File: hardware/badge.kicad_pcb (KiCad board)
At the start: 2 copper layers, 151.5 x 81.5 mm, 52 parts, among them J1 Micro_SD_Card, J2 Conn_01x40, J3 Conn_01x40, SW1 SW_Push, SW10 SW_Push, SW11 SW_Push, SW12 SW_Push, SW13 SW_Push, SW14 SW_Push, SW15 SW_Push, SW16 SW_Push, SW17 SW_Push, SW18 SW_Push, SW19 SW_Push, SW2 SW_Push, SW20 SW_Push, SW21 SW_Push, SW22 SW_Push, SW23 SW_Push, SW24 SW_Push, SW25 SW_Push, SW26 SW_Push, SW27 SW_Push, SW28 SW_Push, SW29 SW_Push, SW3 SW_Push, SW30 SW_Push, SW31 SW_Push, SW32 SW_Push, SW33 SW_Push, SW34 SW_Push, SW35 SW_Push, SW36 SW_Push, SW37 SW_Push, SW38 SW_Push, SW39 SW_Push, SW4 SW_Push, SW40 SW_Push, SW5 SW_Push, SW6 SW_Push, SW7 SW_Push, SW8 SW_Push, SW9 SW_Push, U1 ESP32-S3-WROOM-1

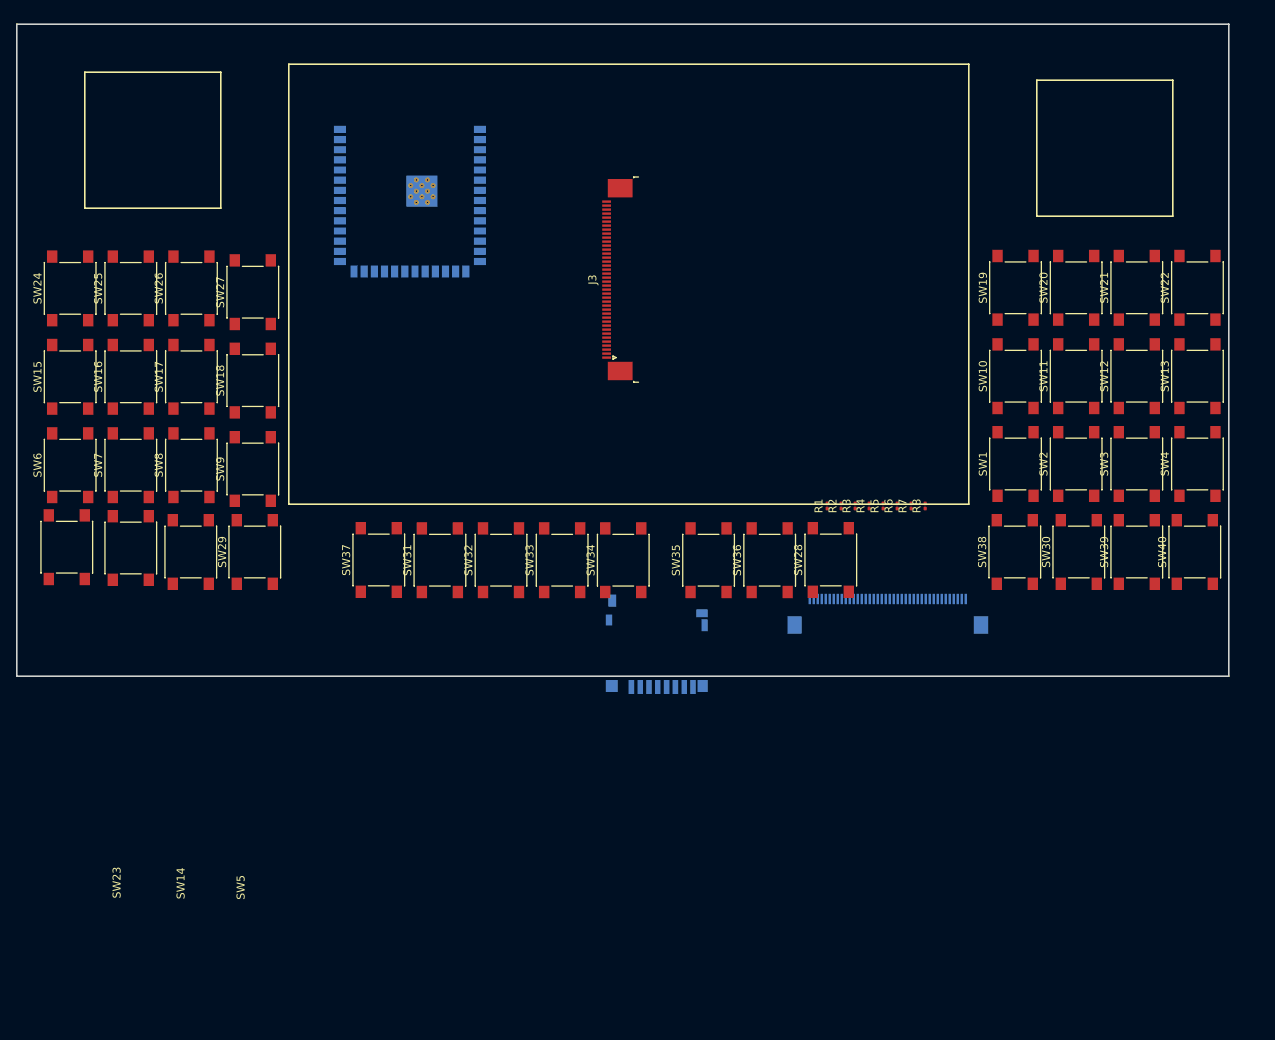
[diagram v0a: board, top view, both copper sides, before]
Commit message: display, switches, (switch)joystick footprint
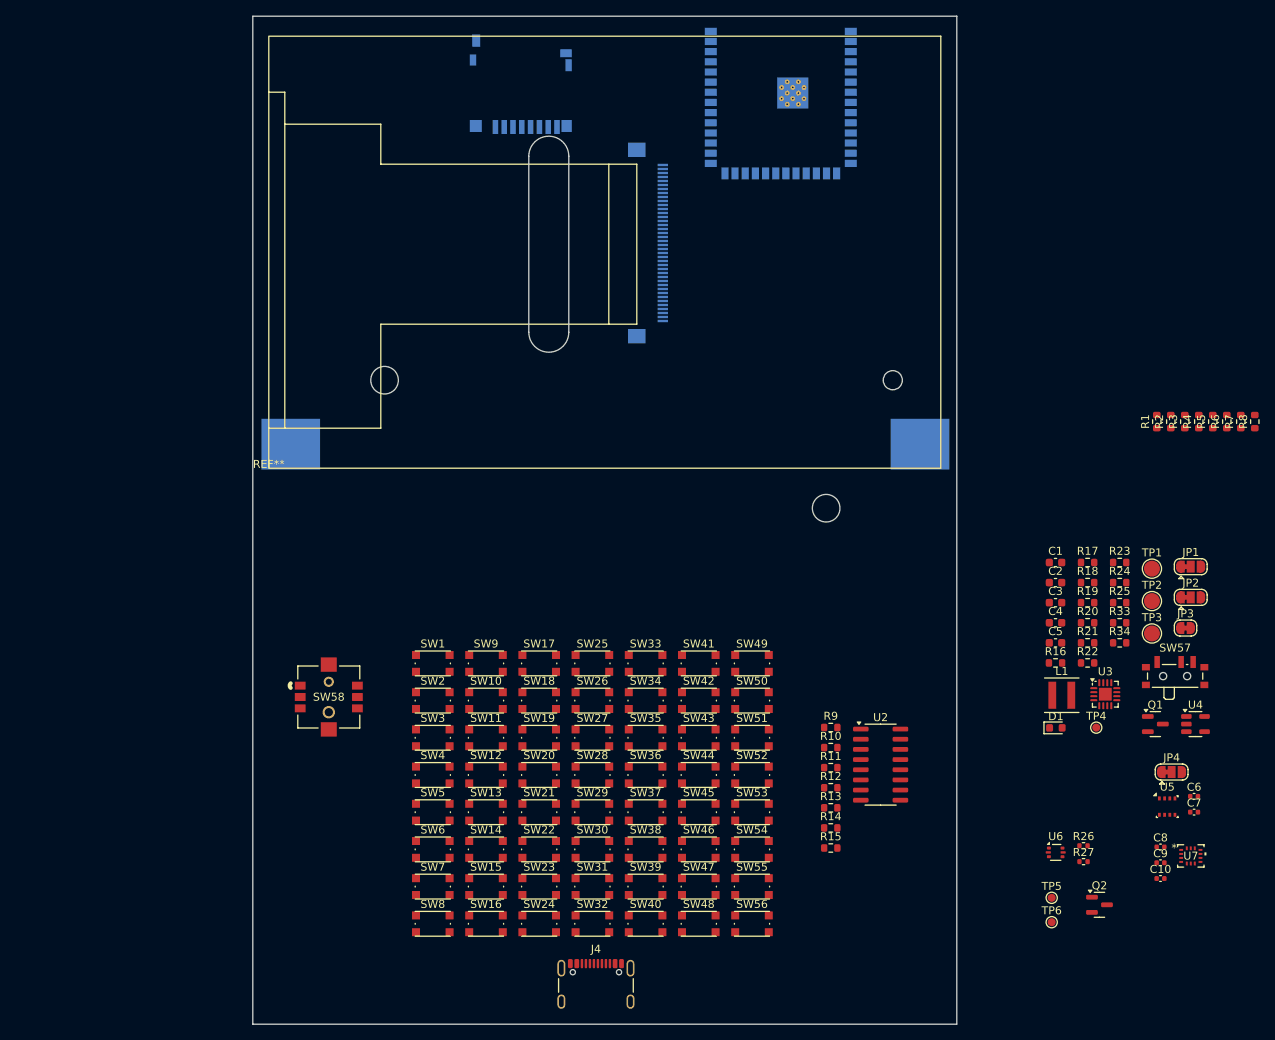
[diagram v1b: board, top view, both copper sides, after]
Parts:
- added C1: 4.7uF, Capacitor_SMD:C_0603_1608Metric, F.Cu at (181.3, 99.3)
- added C10: 100nF 6.3V, Capacitor_SMD:C_0402_1005Metric, F.Cu at (194.5, 138.8)
- added C2: TBD, Capacitor_SMD:C_0603_1608Metric, F.Cu at (181.3, 101.8)
- added C3: 4.7uF, Capacitor_SMD:C_0603_1608Metric, F.Cu at (181.3, 104.3)
- added C4: 10uF, Capacitor_SMD:C_0603_1608Metric, F.Cu at (181.3, 106.8)
- added C5: 4.7uF, Capacitor_SMD:C_0603_1608Metric, F.Cu at (181.3, 109.3)
- added C6: 100nF 6.3V, Capacitor_SMD:C_0402_1005Metric, F.Cu at (198.7, 128.5)
- added C7: 100nF 6.3V, Capacitor_SMD:C_0402_1005Metric, F.Cu at (198.7, 130.5)
- added C8: 1uF 25V, Capacitor_SMD:C_0402_1005Metric, F.Cu at (194.5, 134.8)
- added C9: 100nF 6.3V, Capacitor_SMD:C_0402_1005Metric, F.Cu at (194.5, 136.8)
- added D1: LED, LED_SMD:LED_0603_1608Metric, F.Cu at (181.4, 120.0)
- added J4: USB_C_Receptacle_USB2.0_14P, Connector_USB:USB_C_Receptacle_GCT_USB4105-xx-A_16P_TopMnt_Horizontal, F.Cu at (123.9, 153.1)
- added JP1: EN1, Jumper:SolderJumper-3_P1.3mm_Bridged12_RoundedPad1.0x1.5mm, F.Cu at (198.2, 99.8)
- added JP2: EN2, Jumper:SolderJumper-3_P1.3mm_Bridged12_RoundedPad1.0x1.5mm, F.Cu at (198.2, 103.6)
- added JP3: Grumpy wifasoi jumper, Jumper:SolderJumper-2_P1.3mm_Bridged_RoundedPad1.0x1.5mm, F.Cu at (197.6, 107.5)
- added JP4: SolderJumper_3_Bridged12, Jumper:SolderJumper-3_P1.3mm_Bridged12_RoundedPad1.0x1.5mm, F.Cu at (195.9, 125.5)
- added L1: 2.2uH, Inductor_SMD:L_Coilcraft_XxL4040, F.Cu at (182.1, 115.9)
- added Q1: NPN SS8050, Package_TO_SOT_SMD:SOT-23, F.Cu at (193.8, 119.5)
- added Q2: AO3400A, Package_TO_SOT_SMD:SOT-23, F.Cu at (186.8, 142.1)
- added R10: 22, Resistor_SMD:R_0603_1608Metric, F.Cu at (153.2, 122.4)
- added R11: 22, Resistor_SMD:R_0603_1608Metric, F.Cu at (153.2, 124.9)
- added R12: 22, Resistor_SMD:R_0603_1608Metric, F.Cu at (153.2, 127.4)
- added R13: 22, Resistor_SMD:R_0603_1608Metric, F.Cu at (153.2, 130.0)
- added R14: 22, Resistor_SMD:R_0603_1608Metric, F.Cu at (153.2, 132.5)
- added R15: 22, Resistor_SMD:R_0603_1608Metric, F.Cu at (153.2, 135.0)
- added R16: 0R, Resistor_SMD:R_0603_1608Metric, F.Cu at (181.3, 111.8)
- added R17: TBD, Resistor_SMD:R_0603_1608Metric, F.Cu at (185.4, 99.3)
- added R18: TBD, Resistor_SMD:R_0603_1608Metric, F.Cu at (185.4, 101.8)
- added R19: 10k, Resistor_SMD:R_0603_1608Metric, F.Cu at (185.4, 104.3)
- added R20: 10k, Resistor_SMD:R_0603_1608Metric, F.Cu at (185.4, 106.8)
- added R21: 680k, Resistor_SMD:R_0603_1608Metric, F.Cu at (185.4, 109.3)
- added R22: 150K, Resistor_SMD:R_0603_1608Metric, F.Cu at (185.4, 111.8)
- added R23: 330, Resistor_SMD:R_0603_1608Metric, F.Cu at (189.4, 99.3)
- added R24: 10k, Resistor_SMD:R_0603_1608Metric, F.Cu at (189.4, 101.8)
- added R25: 10k, Resistor_SMD:R_0603_1608Metric, F.Cu at (189.4, 104.3)
- added R26: 5k1, Resistor_SMD:R_0402_1005Metric, F.Cu at (184.8, 134.7)
- added R27: 5k1, Resistor_SMD:R_0402_1005Metric, F.Cu at (184.8, 136.7)
- added R33: 150K, Resistor_SMD:R_0603_1608Metric, F.Cu at (189.4, 106.8)
- added R34: 150K, Resistor_SMD:R_0603_1608Metric, F.Cu at (189.4, 109.3)
- added R9: 22, Resistor_SMD:R_0603_1608Metric, F.Cu at (153.2, 119.9)
- added REF**: display, lib:display, F.Cu at (83.0, 87.5)
- added SW41: SW_Push, lib:bottonepiccolo_C2888430, F.Cu at (136.8, 111.9)
- added SW42: SW_Push, lib:bottonepiccolo_C2888430, F.Cu at (136.8, 116.5)
- added SW43: SW_Push, lib:bottonepiccolo_C2888430, F.Cu at (136.8, 121.2)
- added SW44: SW_Push, lib:bottonepiccolo_C2888430, F.Cu at (136.8, 125.8)
- added SW45: SW_Push, lib:bottonepiccolo_C2888430, F.Cu at (136.8, 130.5)
- added SW46: SW_Push, lib:bottonepiccolo_C2888430, F.Cu at (136.8, 135.2)
- added SW47: SW_Push, lib:bottonepiccolo_C2888430, F.Cu at (136.8, 139.8)
- added SW48: SW_Push, lib:bottonepiccolo_C2888430, F.Cu at (136.8, 144.4)
- added SW49: SW_Push, lib:bottonepiccolo_C2888430, F.Cu at (143.4, 111.9)
- added SW50: SW_Push, lib:bottonepiccolo_C2888430, F.Cu at (143.4, 116.5)
- added SW51: SW_Push, lib:bottonepiccolo_C2888430, F.Cu at (143.4, 121.2)
- added SW52: SW_Push, lib:bottonepiccolo_C2888430, F.Cu at (143.4, 125.8)
- added SW53: SW_Push, lib:bottonepiccolo_C2888430, F.Cu at (143.4, 130.5)
- added SW54: SW_Push, lib:bottonepiccolo_C2888430, F.Cu at (143.4, 135.2)
- added SW55: SW_Push, lib:bottonepiccolo_C2888430, F.Cu at (143.4, 139.8)
- added SW56: SW_Push, lib:bottonepiccolo_C2888430, F.Cu at (143.4, 144.4)
- added SW57: MK-12C02-G020, Button_Switch_SMD:SW_SPDT_PCM12, F.Cu at (196.3, 113.2)
- added SW58: SKRHABE010, lib:SKRHABE010_ALPS, F.Cu at (90.5, 116.1)
- added TP1: TestPoint, TestPoint:TestPoint_Pad_D2.0mm, F.Cu at (193.4, 100.1)
- added TP2: TestPoint, TestPoint:TestPoint_Pad_D2.0mm, F.Cu at (193.4, 104.1)
- added TP3: TestPoint, TestPoint:TestPoint_Pad_D2.0mm, F.Cu at (193.4, 108.2)
- added TP4: TestPoint, TestPoint:TestPoint_Pad_D1.0mm, F.Cu at (186.4, 119.9)
- added TP5: TestPoint, TestPoint:TestPoint_Pad_D1.0mm, F.Cu at (180.9, 141.2)
- added TP6: TestPoint, TestPoint:TestPoint_Pad_D1.0mm, F.Cu at (180.9, 144.2)
- added U2: 74HC138, Package_SO:SOIC-16_3.9x9.9mm_P1.27mm, F.Cu at (159.5, 124.6)
- added U3: BQ24075RGT, Package_DFN_QFN:VQFN-16-1EP_3x3mm_P0.5mm_EP1.6x1.6mm, F.Cu at (187.6, 115.8)
- added U4: TLV62569DBV, Package_TO_SOT_SMD:SOT-23-5, F.Cu at (198.8, 119.5)
- added U5: BME280, Package_LGA:Bosch_LGA-8_2.5x2.5mm_P0.65mm_ClockwisePinNumbering, F.Cu at (195.3, 129.8)
- added U6: USBLC6-2P6, Package_TO_SOT_SMD:SOT-666, F.Cu at (181.4, 135.5)
- added U7: BMI270, footprints:BMI270_BOS, F.Cu at (198.3, 136.0)
- J2: value Conn_01x40 -> batt; footprint Connector_FFC-FPC:Hirose_FH12-40S-0.5SH_1x40-1MP_P0.50mm_Horizontal -> Battery:BatteryHolder_Keystone_1042_1x18650
- J3: footprint Connector_FFC-FPC:TE_4-1734839-0_1x40-1MP_P0.5mm_Horizontal -> Connector_FFC-FPC:Hirose_FH12-40S-0.5SH_1x40-1MP_P0.50mm_Horizontal; moved to B.Cu
- R1, R2: value R -> 10k; footprint Resistor_SMD:R_0201_0603Metric -> Resistor_SMD:R_0603_1608Metric
- R3, R4, R5, R6, R7: footprint Resistor_SMD:R_0201_0603Metric -> Resistor_SMD:R_0603_1608Metric
- R8: value 10k -> 22; footprint Resistor_SMD:R_0201_0603Metric -> Resistor_SMD:R_0603_1608Metric
- SW1, SW10, SW11, SW12, SW13, SW14, SW15, SW16, SW17, SW18, SW19, SW2, SW20, SW21, SW22, SW23, SW24, SW25, SW26, SW27, SW28, SW29, SW3, SW30, SW31, SW32, SW33, SW34, SW35, SW36, SW37, SW38, SW39, SW4, SW40, SW5, SW6, SW7, SW8, SW9: footprint Button_Switch_SMD:SW_Push_1P1T_NO_6x6mm_H9.5mm -> lib:bottonepiccolo_C2888430
- moved SW22 108.2 mm to (116.8, 135.2), turned to 0 degrees
- moved SW13 104.3 mm to (110.2, 130.5), turned to 0 degrees
- moved SW4 103.2 mm to (103.5, 125.8), turned to 0 degrees
- moved SW21 99.4 mm to (116.8, 130.5), turned to 0 degrees
- moved SW24 98.7 mm to (116.8, 144.4), turned to 0 degrees
- moved SW12 95.4 mm to (110.2, 125.8), turned to 0 degrees
- moved SW3 94.4 mm to (103.5, 121.2), turned to 0 degrees
- moved SW20 90.6 mm to (116.8, 125.8), turned to 0 degrees
- moved SW11 86.5 mm to (110.2, 121.2), turned to 0 degrees
- moved SW2 85.7 mm to (103.5, 116.5), turned to 0 degrees
- moved SW40 82.9 mm to (130.1, 144.4), turned to 0 degrees
- moved SW15 82.2 mm to (110.2, 139.8), turned to 0 degrees
- moved SW19 81.9 mm to (116.8, 121.2), turned to 0 degrees
- moved SW16 81.5 mm to (110.2, 144.4), turned to 0 degrees
- moved SW10 77.6 mm to (110.2, 116.5), turned to 0 degrees
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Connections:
- J2 pad 1: unconnected-(J2-Pin_1-Pad1) -> GND
- J2 pad 2: unconnected-(J2-Pin_2-Pad2) -> Net-(J2-Pin_2)
- J3 pad 10: unconnected-(J3-Pin_10-Pad10) -> GND
- J3 pad 11: unconnected-(J3-Pin_11-Pad11) -> /lcd/SPI_CLK
- J3 pad 12: unconnected-(J3-Pin_12-Pad12) -> GND
- J3 pad 13: unconnected-(J3-Pin_13-Pad13) -> /lcd/SPI_MOSI
- J3 pad 14: unconnected-(J3-Pin_14-Pad14) -> /lcd/SPI_MISO
- J3 pad 15: unconnected-(J3-Pin_15-Pad15) -> GND
- J3 pad 16: unconnected-(J3-Pin_16-Pad16) -> GND
- J3 pad 17: unconnected-(J3-Pin_17-Pad17) -> GND
- J3 pad 18: unconnected-(J3-Pin_18-Pad18) -> GND
- J3 pad 19: unconnected-(J3-Pin_19-Pad19) -> GND
- J3 pad 20: unconnected-(J3-Pin_20-Pad20) -> GND
- J3 pad 21: unconnected-(J3-Pin_21-Pad21) -> GND
- J3 pad 22: unconnected-(J3-Pin_22-Pad22) -> GND
- J3 pad 23: unconnected-(J3-Pin_23-Pad23) -> GND
- J3 pad 24: unconnected-(J3-Pin_24-Pad24) -> GND
- J3 pad 25: unconnected-(J3-Pin_25-Pad25) -> GND
- J3 pad 26: unconnected-(J3-Pin_26-Pad26) -> GND
- J3 pad 27: unconnected-(J3-Pin_27-Pad27) -> GND
- J3 pad 28: unconnected-(J3-Pin_28-Pad28) -> GND
- J3 pad 29: unconnected-(J3-Pin_29-Pad29) -> GND
- J3 pad 30: unconnected-(J3-Pin_30-Pad30) -> GND
- J3 pad 31: unconnected-(J3-Pin_31-Pad31) -> GND
- J3 pad 32: unconnected-(J3-Pin_32-Pad32) -> GND
- J3 pad 33: unconnected-(J3-Pin_33-Pad33) -> +3.3V
- J3 pad 34: unconnected-(J3-Pin_34-Pad34) -> /lcd/LEDK
- J3 pad 35: unconnected-(J3-Pin_35-Pad35) -> /lcd/LEDK
- J3 pad 36: unconnected-(J3-Pin_36-Pad36) -> /lcd/LEDK
- J3 pad 37: unconnected-(J3-Pin_37-Pad37) -> GND
- J3 pad 38: unconnected-(J3-Pin_38-Pad38) -> /lcd/IM0
- J3 pad 39: unconnected-(J3-Pin_39-Pad39) -> /lcd/IM1
- J3 pad 40: unconnected-(J3-Pin_40-Pad40) -> /lcd/IM2
- J3 pad 5: unconnected-(J3-Pin_5-Pad5) -> GND
- J3 pad 6: unconnected-(J3-Pin_6-Pad6) -> +3.3V
- J3 pad 7: unconnected-(J3-Pin_7-Pad7) -> +3.3V
- J3 pad 8: unconnected-(J3-Pin_8-Pad8) -> /lcd/FMARK
- J3 pad 9: unconnected-(J3-Pin_9-Pad9) -> /lcd/SPI_CS
- R1 pad 1: Net-(J3-CC1) -> +3.3V
- R1 pad 2: GND -> Net-(U1-EN)
- R2 pad 1: Net-(J3-CC2) -> +3.3V
- R2 pad 2: GND -> Net-(J1-DAT1)
- R3 pad 2: Net-(J1-DAT1) -> /mcu/SD_D0
- R4 pad 2: /mcu/SD_D0 -> /mcu/SD_CLK
- R5 pad 2: /mcu/SD_CLK -> /mcu/SD_CMD
- R6 pad 2: /mcu/SD_CMD -> Net-(J1-DAT3/CD)
- R7 pad 2: Net-(J1-DAT3/CD) -> Net-(J1-DAT2)
- R8 pad 1: +3.3V -> Net-(U2-~{Y0})
- R8 pad 2: Net-(J1-DAT2) -> Net-(R8-Pad2)
- SW1 pad 1: unconnected-(SW1-Pad1) -> Net-(R8-Pad2)
- SW1 pad 2: unconnected-(SW1-Pad2) -> /keyboard/KB_COL0
- SW10 pad 1: unconnected-(SW10-Pad1) -> Net-(R9-Pad2)
- SW10 pad 2: unconnected-(SW10-Pad2) -> /keyboard/KB_COL1
- SW11 pad 1: unconnected-(SW11-Pad1) -> Net-(R10-Pad2)
- SW11 pad 2: unconnected-(SW11-Pad2) -> /keyboard/KB_COL1
- SW12 pad 1: unconnected-(SW12-Pad1) -> Net-(R11-Pad2)
- SW12 pad 2: unconnected-(SW12-Pad2) -> /keyboard/KB_COL1
- SW13 pad 1: unconnected-(SW13-Pad1) -> Net-(R12-Pad2)
- SW13 pad 2: unconnected-(SW13-Pad2) -> /keyboard/KB_COL1
- SW14 pad 1: unconnected-(SW14-Pad1) -> Net-(R13-Pad2)
- SW14 pad 2: unconnected-(SW14-Pad2) -> /keyboard/KB_COL1
- SW15 pad 1: unconnected-(SW15-Pad1) -> Net-(R14-Pad2)
- SW15 pad 2: unconnected-(SW15-Pad2) -> /keyboard/KB_COL1
- SW16 pad 1: unconnected-(SW16-Pad1) -> Net-(R15-Pad2)
- SW16 pad 2: unconnected-(SW16-Pad2) -> /keyboard/KB_COL1
- SW17 pad 1: unconnected-(SW17-Pad1) -> Net-(R8-Pad2)
- SW17 pad 2: unconnected-(SW17-Pad2) -> /keyboard/KB_COL2
- SW18 pad 1: unconnected-(SW18-Pad1) -> Net-(R9-Pad2)
- SW18 pad 2: unconnected-(SW18-Pad2) -> /keyboard/KB_COL2
- SW19 pad 1: unconnected-(SW19-Pad1) -> Net-(R10-Pad2)
- SW19 pad 2: unconnected-(SW19-Pad2) -> /keyboard/KB_COL2
- SW2 pad 1: unconnected-(SW2-Pad1) -> Net-(R9-Pad2)
- SW2 pad 2: unconnected-(SW2-Pad2) -> /keyboard/KB_COL0
- SW20 pad 1: unconnected-(SW20-Pad1) -> Net-(R11-Pad2)
- SW20 pad 2: unconnected-(SW20-Pad2) -> /keyboard/KB_COL2
- SW21 pad 1: unconnected-(SW21-Pad1) -> Net-(R12-Pad2)
- SW21 pad 2: unconnected-(SW21-Pad2) -> /keyboard/KB_COL2
- SW22 pad 1: unconnected-(SW22-Pad1) -> Net-(R13-Pad2)
- SW22 pad 2: unconnected-(SW22-Pad2) -> /keyboard/KB_COL2
- SW23 pad 1: unconnected-(SW23-Pad1) -> Net-(R14-Pad2)
- SW23 pad 2: unconnected-(SW23-Pad2) -> /keyboard/KB_COL2
- SW24 pad 1: unconnected-(SW24-Pad1) -> Net-(R15-Pad2)
- SW24 pad 2: unconnected-(SW24-Pad2) -> /keyboard/KB_COL2
- SW25 pad 1: unconnected-(SW25-Pad1) -> Net-(R8-Pad2)
- SW25 pad 2: unconnected-(SW25-Pad2) -> /keyboard/KB_COL3
- SW26 pad 1: unconnected-(SW26-Pad1) -> Net-(R9-Pad2)
- SW26 pad 2: unconnected-(SW26-Pad2) -> /keyboard/KB_COL3
- SW27 pad 1: unconnected-(SW27-Pad1) -> Net-(R10-Pad2)
- SW27 pad 2: unconnected-(SW27-Pad2) -> /keyboard/KB_COL3
- SW28 pad 1: unconnected-(SW28-Pad1) -> Net-(R11-Pad2)
- SW28 pad 2: unconnected-(SW28-Pad2) -> /keyboard/KB_COL3
- SW29 pad 1: unconnected-(SW29-Pad1) -> Net-(R12-Pad2)
- SW29 pad 2: unconnected-(SW29-Pad2) -> /keyboard/KB_COL3
- SW3 pad 1: unconnected-(SW3-Pad1) -> Net-(R10-Pad2)
- SW3 pad 2: unconnected-(SW3-Pad2) -> /keyboard/KB_COL0
- SW30 pad 1: unconnected-(SW30-Pad1) -> Net-(R13-Pad2)
- SW30 pad 2: unconnected-(SW30-Pad2) -> /keyboard/KB_COL3
- SW31 pad 1: unconnected-(SW31-Pad1) -> Net-(R14-Pad2)
- SW31 pad 2: unconnected-(SW31-Pad2) -> /keyboard/KB_COL3
- SW32 pad 1: unconnected-(SW32-Pad1) -> Net-(R15-Pad2)
- SW32 pad 2: unconnected-(SW32-Pad2) -> /keyboard/KB_COL3
- SW33 pad 1: unconnected-(SW33-Pad1) -> Net-(R8-Pad2)
- SW33 pad 2: unconnected-(SW33-Pad2) -> /keyboard/KB_COL4
- SW34 pad 1: unconnected-(SW34-Pad1) -> Net-(R9-Pad2)
- SW34 pad 2: unconnected-(SW34-Pad2) -> /keyboard/KB_COL4
- SW35 pad 1: unconnected-(SW35-Pad1) -> Net-(R10-Pad2)
- SW35 pad 2: unconnected-(SW35-Pad2) -> /keyboard/KB_COL4
- SW36 pad 1: unconnected-(SW36-Pad1) -> Net-(R11-Pad2)
- SW36 pad 2: unconnected-(SW36-Pad2) -> /keyboard/KB_COL4
- SW37 pad 1: unconnected-(SW37-Pad1) -> Net-(R12-Pad2)
- SW37 pad 2: unconnected-(SW37-Pad2) -> /keyboard/KB_COL4
- SW38 pad 1: unconnected-(SW38-Pad1) -> Net-(R13-Pad2)
- SW38 pad 2: unconnected-(SW38-Pad2) -> /keyboard/KB_COL4
- SW39 pad 1: unconnected-(SW39-Pad1) -> Net-(R14-Pad2)
- SW39 pad 2: unconnected-(SW39-Pad2) -> /keyboard/KB_COL4
- SW4 pad 1: unconnected-(SW4-Pad1) -> Net-(R11-Pad2)
- SW4 pad 2: unconnected-(SW4-Pad2) -> /keyboard/KB_COL0
- SW40 pad 1: unconnected-(SW40-Pad1) -> Net-(R15-Pad2)
- SW40 pad 2: unconnected-(SW40-Pad2) -> /keyboard/KB_COL4
- SW5 pad 1: unconnected-(SW5-Pad1) -> Net-(R12-Pad2)
- SW5 pad 2: unconnected-(SW5-Pad2) -> /keyboard/KB_COL0
- SW6 pad 1: unconnected-(SW6-Pad1) -> Net-(R13-Pad2)
- SW6 pad 2: unconnected-(SW6-Pad2) -> /keyboard/KB_COL0
- SW7 pad 1: unconnected-(SW7-Pad1) -> Net-(R14-Pad2)
- SW7 pad 2: unconnected-(SW7-Pad2) -> /keyboard/KB_COL0
- SW8 pad 1: unconnected-(SW8-Pad1) -> Net-(R15-Pad2)
- SW8 pad 2: unconnected-(SW8-Pad2) -> /keyboard/KB_COL0
- SW9 pad 1: unconnected-(SW9-Pad1) -> Net-(R8-Pad2)
- SW9 pad 2: unconnected-(SW9-Pad2) -> /keyboard/KB_COL1
- U1 pad 1: Net-(U1-GND-Pad1) -> GND
- U1 pad 10: unconnected-(U1-IO17-Pad10) -> /mcu/VBAT_DIV2
- U1 pad 12: unconnected-(U1-IO8-Pad12) -> /keyboard/KB_COL0
- U1 pad 13: unconnected-(U1-IO19-Pad13) -> /mcu/USB_D-
- U1 pad 14: unconnected-(U1-IO20-Pad14) -> /mcu/USB_D+
- U1 pad 15: unconnected-(U1-IO3-Pad15) -> /mcu/SD_D0
- U1 pad 17: unconnected-(U1-IO9-Pad17) -> /keyboard/KB_COL1
- U1 pad 18: unconnected-(U1-IO10-Pad18) -> /keyboard/KB_COL2
- U1 pad 19: unconnected-(U1-IO11-Pad19) -> /keyboard/KB_COL3
- U1 pad 2: unconnected-(U1-3V3-Pad2) -> +3.3V
- U1 pad 20: unconnected-(U1-IO12-Pad20) -> /keyboard/KB_COL4
- U1 pad 21: unconnected-(U1-IO13-Pad21) -> /keyboard/KB_COL5
- U1 pad 22: unconnected-(U1-IO14-Pad22) -> /keyboard/KB_COL6
- U1 pad 23: unconnected-(U1-IO21-Pad23) -> GND
- U1 pad 24: unconnected-(U1-IO47-Pad24) -> /imu/SDA
- U1 pad 25: unconnected-(U1-IO48-Pad25) -> /imu/SCL
- U1 pad 27: unconnected-(U1-IO0-Pad27) -> /mcu/IO0
- U1 pad 3: unconnected-(U1-EN-Pad3) -> Net-(U1-EN)
- U1 pad 31: unconnected-(U1-IO38-Pad31) -> /lcd/SPI_MOSI
- U1 pad 32: unconnected-(U1-IO39-Pad32) -> /lcd/SPI_MISO
- U1 pad 33: unconnected-(U1-IO40-Pad33) -> /lcd/SPI_CLK
- U1 pad 34: unconnected-(U1-IO41-Pad34) -> /lcd/SPI_CS
- U1 pad 35: unconnected-(U1-IO42-Pad35) -> /lcd/BACKLIGHT
- U1 pad 38: unconnected-(U1-IO2-Pad38) -> /mcu/SD_CLK
- U1 pad 39: unconnected-(U1-IO1-Pad39) -> /mcu/SD_CMD
- U1 pad 4: unconnected-(U1-IO4-Pad4) -> /mcu/CHG
- U1 pad 40: Net-(U1-GND-Pad1) -> GND
- U1 pad 41: Net-(U1-GND-Pad1) -> GND
- U1 pad 5: unconnected-(U1-IO5-Pad5) -> /keyboard/KB_ROW0
- U1 pad 6: unconnected-(U1-IO6-Pad6) -> /keyboard/KB_ROW1
- U1 pad 7: unconnected-(U1-IO7-Pad7) -> /keyboard/KB_ROW2
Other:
- board size 151.5 x 81.5 mm -> 88 x 126 mm

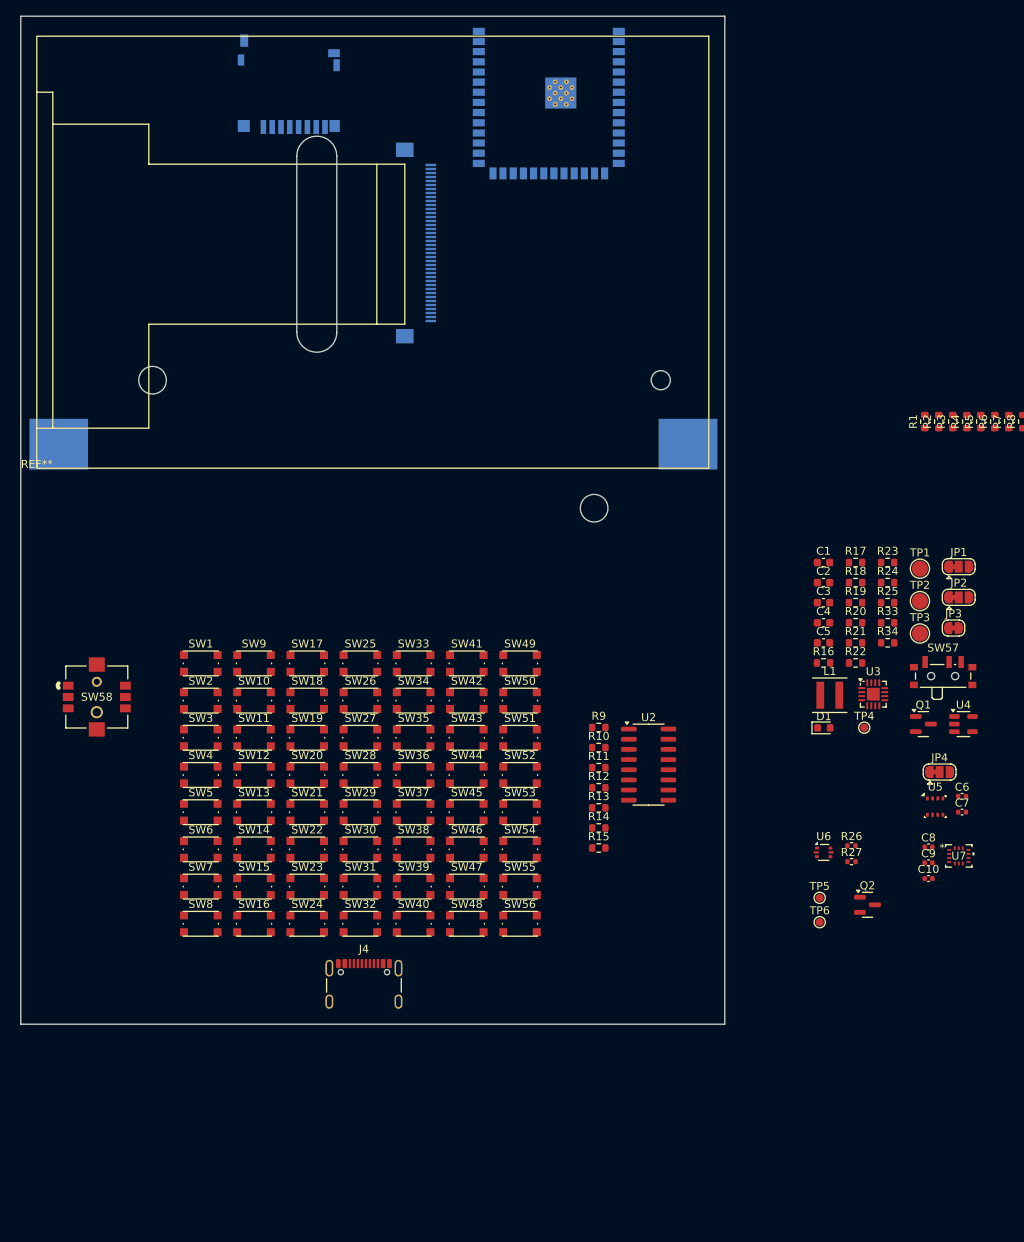
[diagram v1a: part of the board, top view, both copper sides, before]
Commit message: joystick collegato, tastiera aggiornata, modulo lora, layout preliminare
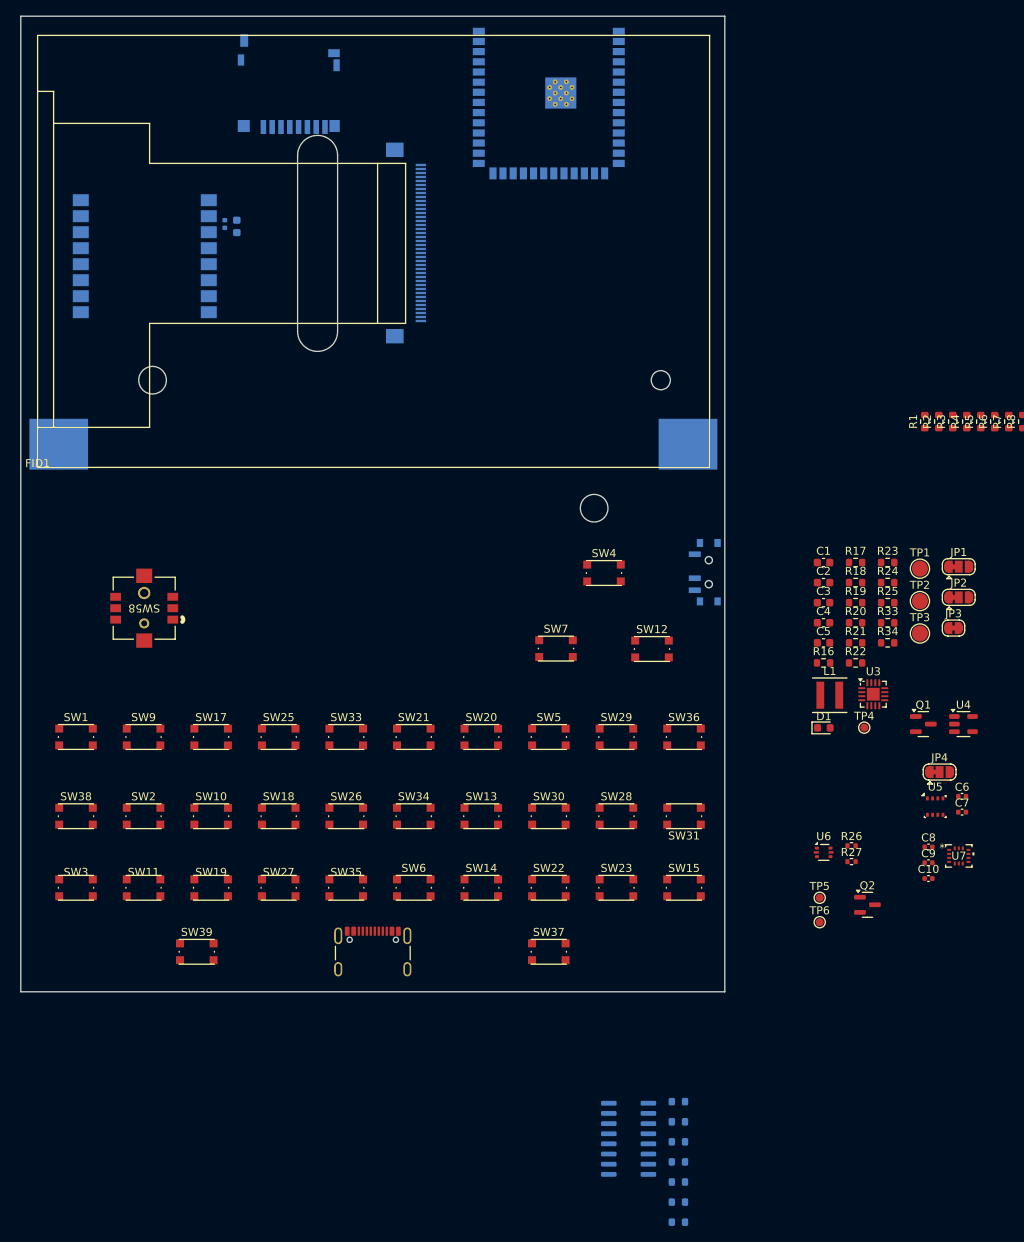
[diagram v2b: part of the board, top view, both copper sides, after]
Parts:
- removed REF**: display, lib:display
- removed SW16, SW24, SW32, SW40, SW41, SW42, SW43, SW44, SW45, SW46, SW47, SW48, SW49, SW50, SW51, SW52, SW53, SW54, SW55, SW56, SW8: SW_Push, lib:bottonepiccolo_C2888430
- added C11: 100nF 6.3V, Capacitor_SMD:C_0402_1005Metric, B.Cu at (106.5, 57.0)
- added C12: 10uF, Capacitor_SMD:C_0603_1608Metric, B.Cu at (108.0, 57.3)
- added FID1: DISPLAY, lib:display, F.Cu at (83.1, 87.4)
- added U8: Ai-Thinker-Ra-02, RF_Module:Ai-Thinker-Ra-01-LoRa, B.Cu at (96.5, 61.0)
- R10, R11, R12, R13, R14, R15, R9, SW57, U2: moved to B.Cu
- moved SW4 56.4 mm to (153.9, 100.6)
- moved SW15 53.8 mm to (163.9, 139.9)
- moved SW7 53.4 mm to (147.9, 110.0)
- moved SW12 52.2 mm to (159.9, 110.1)
- moved R11 47.8 mm to (163.2, 171.7), turned to 180 degrees
- moved R12 47.8 mm to (163.2, 174.2), turned to 180 degrees
- moved R14 47.8 mm to (163.2, 179.2), turned to 180 degrees
- moved R15 47.8 mm to (163.2, 181.7), turned to 180 degrees
- moved R10 47.8 mm to (163.2, 169.2), turned to 180 degrees
- moved R9 47.8 mm to (163.2, 166.7), turned to 180 degrees
- moved R13 47.8 mm to (163.2, 176.7), turned to 180 degrees
- moved U2 46.8 mm to (157.0, 171.3), turned to 180 degrees
- moved SW5 44.5 mm to (147.0, 121.1)
- moved SW38 42.4 mm to (87.9, 131.0)
- moved SW31 41.4 mm to (163.9, 131.0), turned to 180 degrees
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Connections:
- SW58 pad 1: unconnected-(SW58-Pad1) -> /keyboard/KB_COL2
- SW58 pad 2: unconnected-(SW58-Pad2) -> /keyboard/KB_COL3
- SW58 pad 3: unconnected-(SW58-Pad3) -> /keyboard/KB_COL4
- SW58 pad 4: unconnected-(SW58-Pad4) -> /keyboard/KB_COL1
- SW58 pad 5: unconnected-(SW58-Pad5) -> Net-(R15-Pad2)
- SW58 pad 6: unconnected-(SW58-Pad6) -> /keyboard/KB_COL0
- U1 pad 11: unconnected-(U1-IO18-Pad11) -> /mcu/LORA_IRQ
- U1 pad 16: unconnected-(U1-IO46-Pad16) -> /mcu/LORA_CE
- U1 pad 26: unconnected-(U1-IO45-Pad26) -> /mcu/LORA_NSS
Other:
- board size 88 x 126 mm -> 88 x 121.9 mm

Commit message: keyboard demo
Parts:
- removed Q2: AO3400A, Package_TO_SOT_SMD:SOT-23
- added Q3: AO3400A, Package_TO_SOT_SMD:SOT-23, F.Cu at (74.7, 91.5)
- added R28: 0R, lib:SKRHABE010_ALPS, F.Cu at (55.4, 89.0)
- added R35: 10k, Resistor_SMD:R_0603_1608Metric, F.Cu at (63.6, 108.5)
- added SW8: BOOT, lib:bottonepiccolo_C2888430, F.Cu at (64.9, 105.0)
- J4: moved to B.Cu
- Q1: value NPN SS8050 -> AO3400A
- R17: value TBD -> 1.2k
- R18: value TBD -> 1.78k
- moved J2 122.2 mm to (243.4, 54.0)
- moved SW31 8.22 mm to (162.0, 123.0), turned to 0 degrees
- moved SW28 8.17 mm to (153.8, 123.0)
- moved SW15 8.17 mm to (162.0, 132.0)
- moved SW30 8.13 mm to (145.6, 123.0)
- moved SW23 8.13 mm to (153.8, 132.0)
- moved SW13 8.09 mm to (137.3, 123.0)
- moved SW22 8.08 mm to (145.6, 132.0)
- moved SW34 8.06 mm to (129.1, 123.0)
- moved SW14 8.05 mm to (137.3, 132.0)
- moved SW26 8.04 mm to (120.9, 123.0)
- moved SW18 8.02 mm to (112.7, 123.0)
- moved SW6 8.01 mm to (129.1, 132.0)
- moved SW10 8.01 mm to (104.4, 123.0)
- moved SW2 8.00 mm to (96.2, 123.0)
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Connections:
- R34 pad 1: Net-(J2-Pin_2) -> VSYS
- U1 pad 16: /mcu/LORA_CE -> unconnected-(U1-IO46-Pad16)
- U1 pad 21: /keyboard/KB_COL5 -> unconnected-(U1-IO13-Pad21)
- U1 pad 22: /keyboard/KB_COL6 -> unconnected-(U1-IO14-Pad22)
- U1 pad 26: /mcu/LORA_NSS -> unconnected-(U1-IO45-Pad26)
- U1 pad 27: /mcu/IO0 -> Net-(U1-IO0)
- U1 pad 8: unconnected-(U1-IO15-Pad8) -> /mcu/LORA_CE
- U1 pad 9: unconnected-(U1-IO16-Pad9) -> /mcu/LORA_NSS
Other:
- board size 88 x 121.9 mm -> 88 x 115 mm
- board text added: "!"
- board text added: "$"
- board text added: "%"
- board text added: "&"
- board text added: "("
- board text added: ")"
- board text added: "*"
- board text added: "+"
- board text added: ","
- board text added: "-"
- board text added: "."
- board text added: "/"
- board text added: "0"
- board text added: "1"
- board text added: "2"
- board text added: "3"
- board text added: "4"
- board text added: "5"
- board text added: "6"
- board text added: "7"
- board text added: "8"
- board text added: "9"
- board text added: ":"
- board text added: ";"
- board text added: "<"
- board text added: "="
- board text added: ">"
- board text added: "@"
- board text added: "A"
- board text added: "B"
- board text added: "C"
- board text added: "D"
- board text added: "E"
- board text added: "F"
- board text added: "G"
- board text added: "H"
- board text added: "I"
- board text added: "J"
- board text added: "K"
- board text added: "L"
- board text added: "M"
- board text added: "MOD"
- board text added: "N"
- board text added: "O"
- board text added: "P"
- board text added: "Q"
- board text added: "R"
- board text added: "S"
- board text added: "T"
- board text added: "U"
- board text added: "V"
- board text added: "W"
- board text added: "X"
- board text added: "Y"
- board text added: "Z"
- board text added: "_"
- board text added: "`"
- board text added: "{dblquote}"
- board text added: "£"
